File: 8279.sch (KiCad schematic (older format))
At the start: 44 parts, among them SW1 SW_Push, SW10 SW_Push, SW11 SW_Push, SW12 SW_Push, SW13 SW_Push, SW14 SW_Push, SW15 SW_Push, SW16 SW_Push, SW17 SW_Push, SW18 SW_Push, SW19 SW_Push, SW2 SW_Push, SW20 SW_Push, SW3 SW_Push, SW4 SW_Push, SW5 SW_Push, SW6 SW_Push, SW7 SW_Push, SW8 SW_Push, SW9 SW_Push, U1 74HC237, U1 74LS540

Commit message: Merged 8254
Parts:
- gave numbers to parts that had none: 15
- renumbered PKDI to PKDI1, SWCTR to SWCTR1, SWINTR to SWINTR1, SWNMI to SWNMI1, SWRST to SWRST1, SWSHFT to SWSHFT1, U1 to U17, UPKDI to UPKDI1

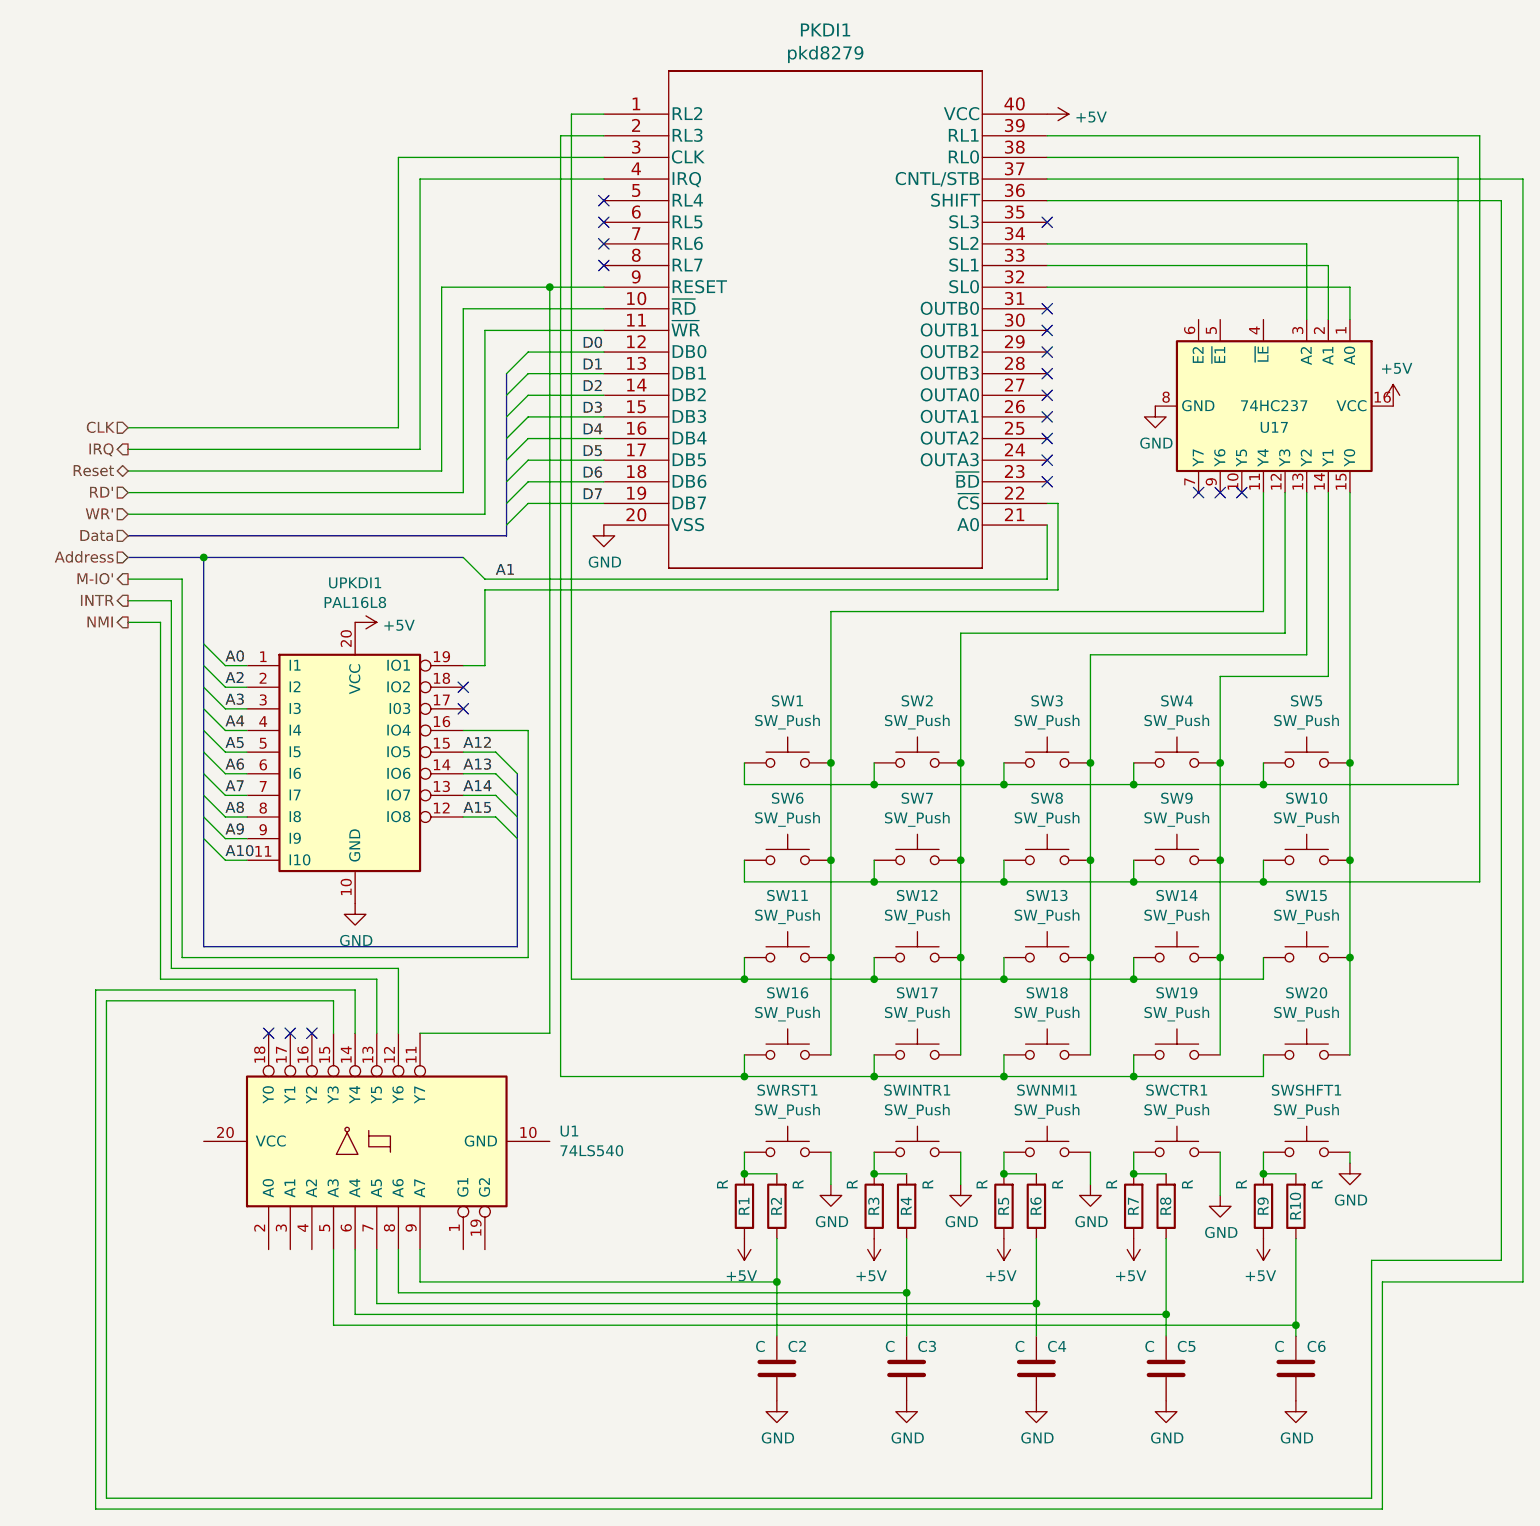
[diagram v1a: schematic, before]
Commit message: Integrated LCD.  Fixed issues with busses
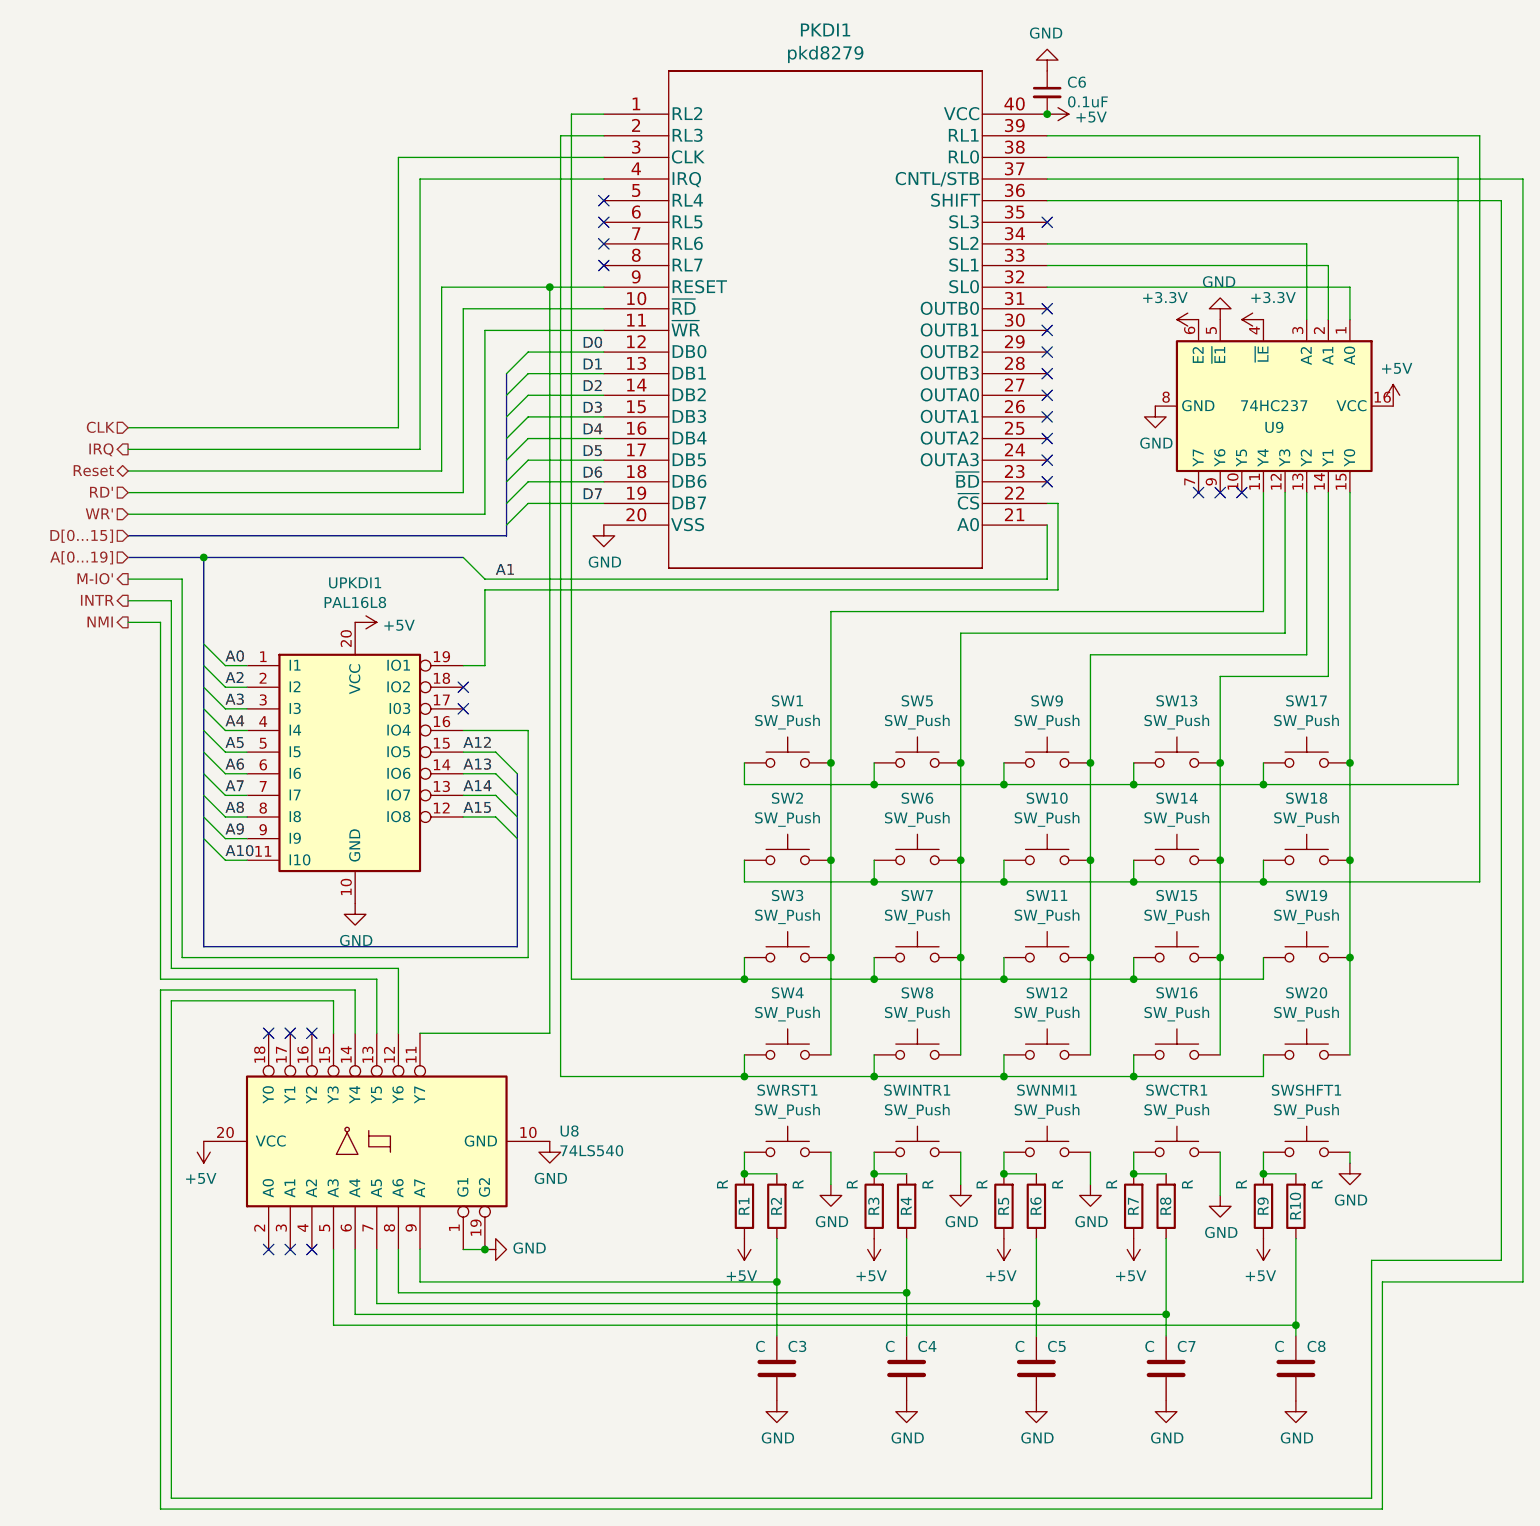
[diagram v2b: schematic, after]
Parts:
- added C6: 0.1uF, symbol Device:C_Small
- renumbered C2 to C3, C3 to C4, C4 to C5, C5 to C7, C6 to C8, SW8 to SW10, SW13 to SW11, SW18 to SW12, SW4 to SW13, SW9 to SW14, SW14 to SW15, SW19 to SW16, SW5 to SW17, SW10 to SW18, SW15 to SW19, SW6 to SW2, SW11 to SW3, SW16 to SW4, SW2 to SW5, SW7 to SW6, SW12 to SW7, SW17 to SW8, SW3 to SW9, U1 to U8, U17 to U9
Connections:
- net +5V: now also U8.20 (VCC), C6.2
- net GND: now also U8.1 (G1), U8.10 (GND), U8.19 (G2), U9.5 (~E1), C6.1
- net +3V3: now reaches U9.4 (~LE)
- net +3V3: now also U9.6 (E2)
- no-connect marks 22 -> 25
